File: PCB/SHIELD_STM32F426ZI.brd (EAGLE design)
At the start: 92.4 x 119.5 mm, 16 parts, among them IC1 AS4C16M16SA-6TCN, J1 104239-1430

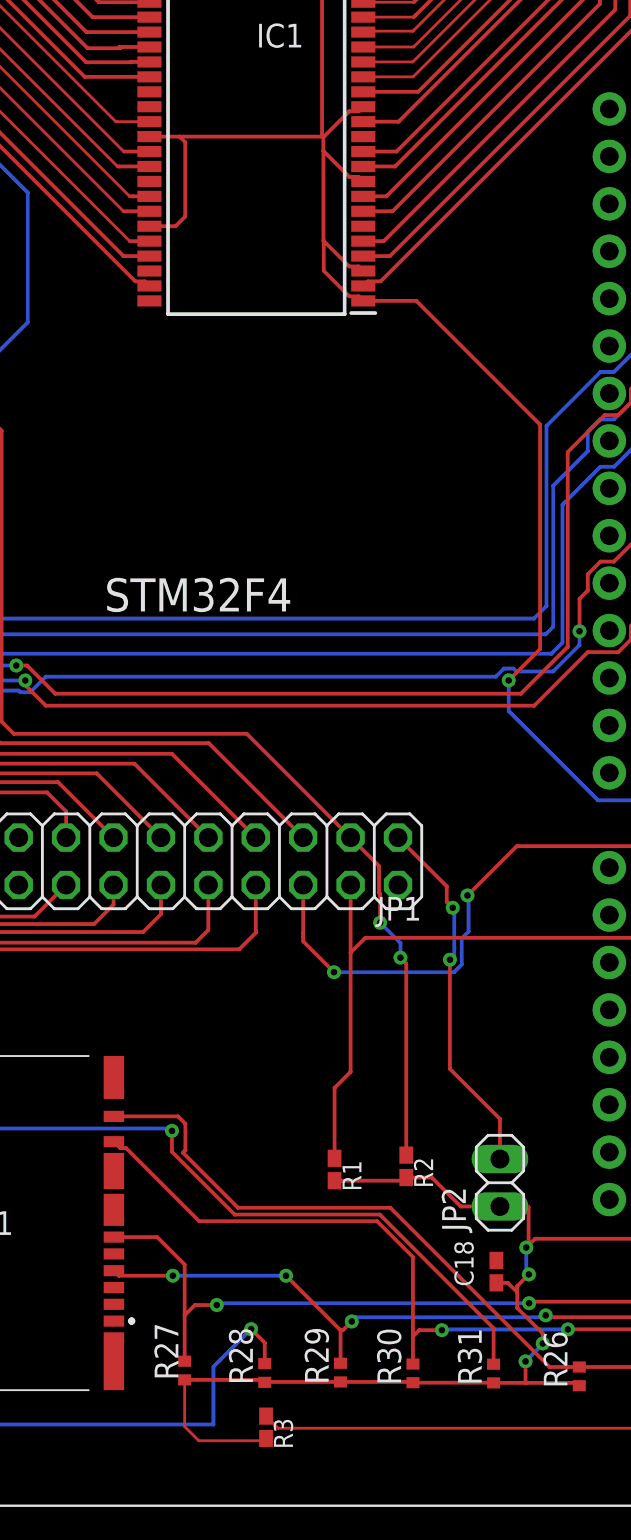
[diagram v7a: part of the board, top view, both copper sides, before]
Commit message: modyfi fault by ERC and DRC
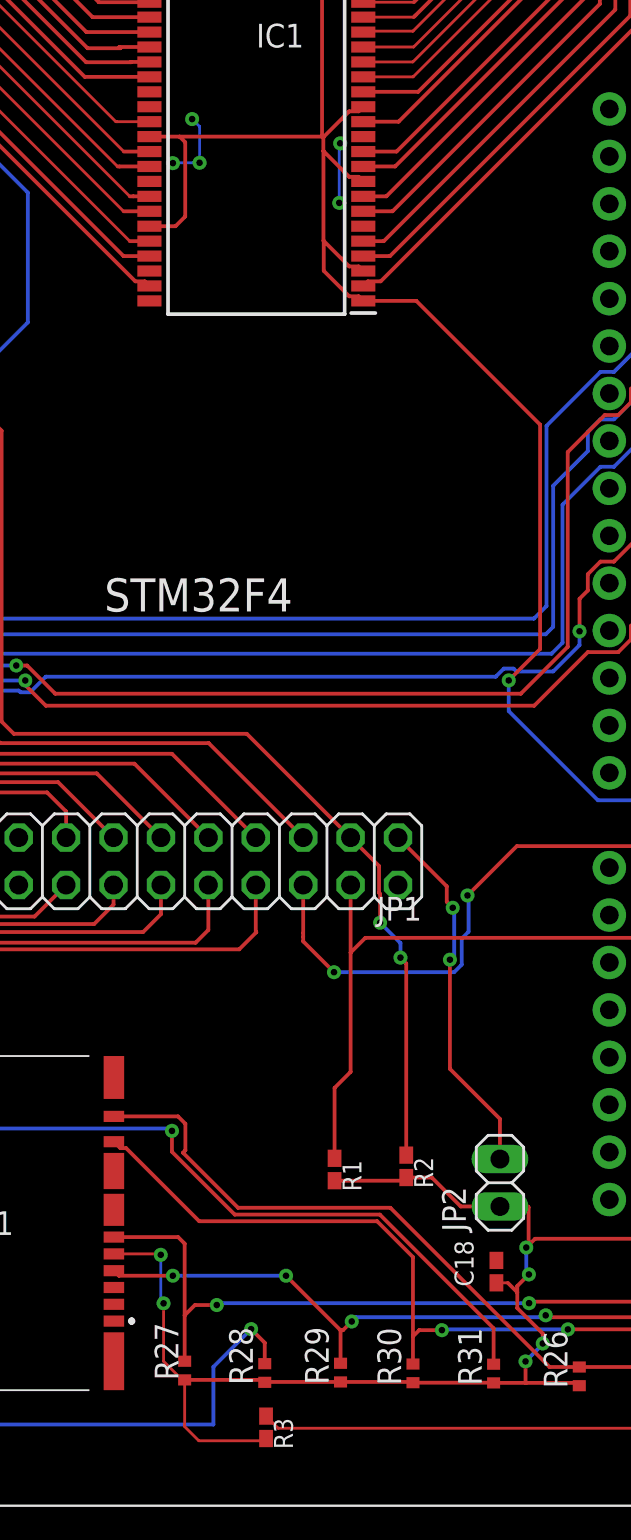
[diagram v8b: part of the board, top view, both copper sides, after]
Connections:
- removed net 3V3: J1.10
- removed net A: STM32F4.CN12_3
- removed net N$107: STM32F4.CN11_65
- removed net N$109: STM32F4.CN11_68
- removed net N$112: STM32F4.CN12_12
- removed net N$114: STM32F4.CN12_14
- removed net N$115: STM32F4.CN12_15
- removed net N$116: STM32F4.CN12_16
- removed net N$118: STM32F4.CN12_18
- removed net N$120: STM32F4.CN12_21
- removed net N$121: STM32F4.CN12_22
- removed net N$123: STM32F4.CN12_24
- removed net N$124: STM32F4.CN12_25
- removed net N$125: STM32F4.CN12_26
- removed net N$126: STM32F4.CN12_27
- removed net N$127: STM32F4.CN12_28
- removed net N$128: STM32F4.CN12_29
- removed net N$129: STM32F4.CN12_30
- removed net N$130: STM32F4.CN12_31
- removed net N$131: STM32F4.CN12_32
- removed net N$132: STM32F4.CN12_33
- removed net N$133: STM32F4.CN12_34
- removed net N$134: STM32F4.CN12_35
- removed net N$136: STM32F4.CN12_37
- removed net N$139: STM32F4.CN12_41
- removed net N$140: STM32F4.CN12_42
- removed net N$141: STM32F4.CN12_43
- removed net N$143: STM32F4.CN12_45
- removed net N$158: STM32F4.CN12_61
- removed net N$163: STM32F4.CN12_67
- removed net N$166: STM32F4.CN12_70
- removed net N$2: STM32F4.CN11_66
- removed net N$41: IC1.40
- removed net N$48: STM32F4.CN12_5
- removed net N$49: STM32F4.CN12_6
- removed net N$50: STM32F4.CN12_7
- removed net N$51: STM32F4.CN12_8
- removed net N$55: STM32F4.CN11_5
- removed net N$56: STM32F4.CN11_6
- removed net N$57: STM32F4.CN11_7
- removed net N$58: STM32F4.CN11_9
- removed net N$59: STM32F4.CN11_11
- removed net N$60: STM32F4.CN11_12
- removed net N$61: STM32F4.CN11_13
- removed net N$62: STM32F4.CN11_14
- removed net N$63: STM32F4.CN11_15
- removed net N$65: STM32F4.CN11_17
- removed net N$66: STM32F4.CN11_18
- removed net N$69: STM32F4.CN11_23
- removed net N$70: STM32F4.CN11_24
- removed net N$71: STM32F4.CN11_25
- removed net N$72: STM32F4.CN11_27
- removed net N$73: STM32F4.CN11_28
- removed net N$74: STM32F4.CN11_29
- removed net N$75: STM32F4.CN11_30
- removed net N$76: STM32F4.CN11_31
- removed net N$78: STM32F4.CN11_33
- removed net N$79: STM32F4.CN11_34
- removed net N$81: STM32F4.CN11_36
- removed net N$84: STM32F4.CN11_39
- removed net N$86: STM32F4.CN11_41
- removed net N$88: STM32F4.CN11_43
- removed net N$89: STM32F4.CN11_44
- removed net N$90: STM32F4.CN11_45
- removed net N$91: STM32F4.CN11_46
- removed net N$92: STM32F4.CN11_47
- removed net N$96: STM32F4.CN12_11
- removed net N$97: STM32F4.CN11_54
- removed net N$99: STM32F4.CN11_56
- removed net PWDN: JP1.18
- removed net RESET: JP1.17
- net 3.3V: now also J1.10
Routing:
- net 3.3V: track 175.5 -> 185.4 mm, vias 6 -> 8
- net GND: track 0.00 -> 7.15 mm, vias 0 -> 5
- net SDIO_CMD: track 41.2 -> 41.8 mm
